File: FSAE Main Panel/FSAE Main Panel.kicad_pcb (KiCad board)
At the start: 2 copper layers, 3 parts

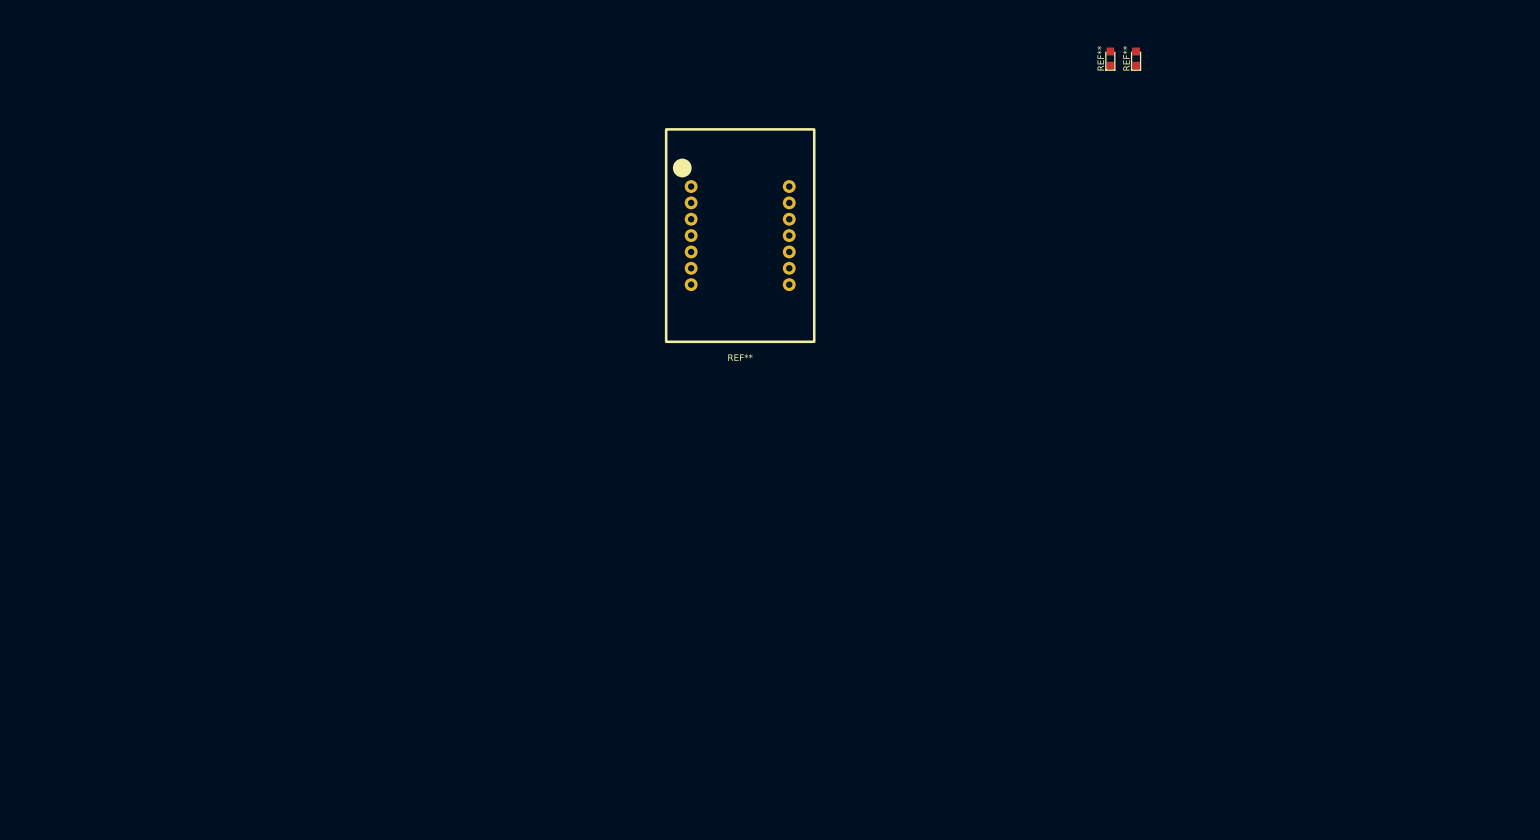
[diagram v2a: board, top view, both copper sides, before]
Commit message: Edited footprints, started PCB layout
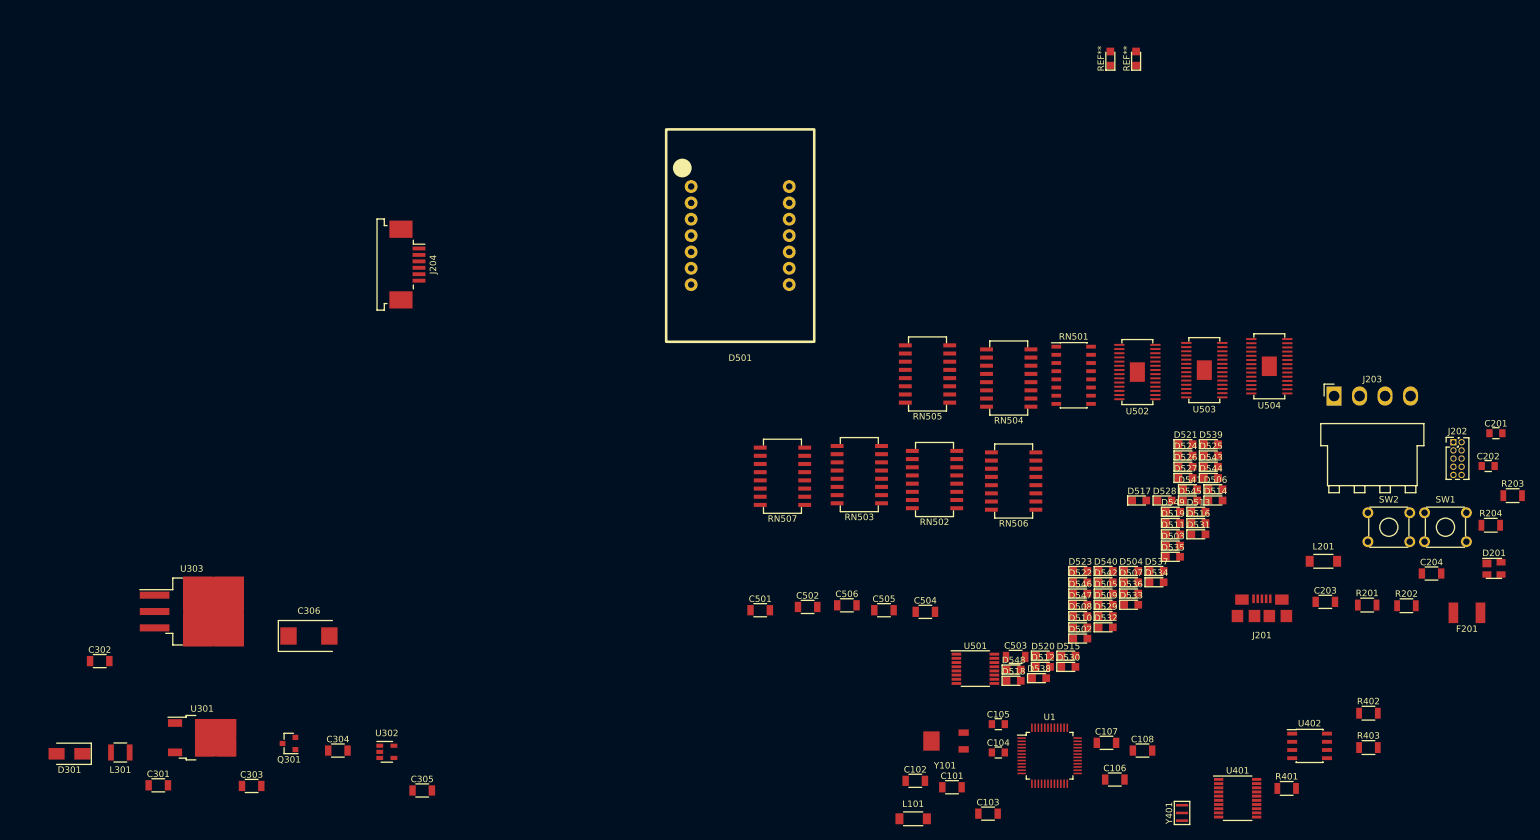
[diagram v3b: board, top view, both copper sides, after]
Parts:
- removed the REF** at (162.5, 65.5)
- added C101: 100nF, Capacitors_SMD:C_1206, F.Cu at (195.4, 151.2)
- added C102: 10uF, Capacitors_SMD:C_1206, F.Cu at (189.7, 150.2)
- added C103: 100nF, Capacitors_SMD:C_1206, F.Cu at (201.0, 155.3)
- added C104: 6.8pF, Capacitors_SMD:C_0805, F.Cu at (202.6, 145.8)
- added C105: 6.8pF, Capacitors_SMD:C_0805, F.Cu at (202.6, 141.4)
- added C106: 100nF, Capacitors_SMD:C_1206, F.Cu at (220.7, 150.0)
- added C107: 100nF, Capacitors_SMD:C_1206, F.Cu at (219.4, 144.3)
- added C108: 100nF, Capacitors_SMD:C_1206, F.Cu at (225.0, 145.5)
- added C201: 100pF, Capacitors_SMD:C_0805, F.Cu at (279.9, 96.2)
- added C202: 100pF, Capacitors_SMD:C_0805, F.Cu at (278.7, 101.3)
- added C203: 4.7nF, Capacitors_SMD:C_1206, F.Cu at (253.4, 122.4)
- added C204: 4.7nF, Capacitors_SMD:C_1206, F.Cu at (269.9, 118.0)
- added C301: 4.7uF, Capacitors_SMD:C_1206, F.Cu at (72.1, 150.9)
- added C302: 10uF, Capacitors_SMD:C_1206, F.Cu at (63.0, 131.6)
- added C303: 4.7uF, Capacitors_SMD:C_1206, F.Cu at (86.6, 151.0)
- added C304: 47uF, Capacitors_SMD:C_1206, F.Cu at (100.0, 145.5)
- added C305: 4.7uF, Capacitors_SMD:C_1206, F.Cu at (113.1, 151.7)
- added C306: 100uF, Capacitors_Tantalum_SMD:CP_Tantalum_Case-D_EIA-7343-31_Reflow, F.Cu at (95.5, 127.7)
- added C501: 1uF, Capacitors_SMD:C_1206, F.Cu at (165.6, 123.7)
- added C502: 100nF, Capacitors_SMD:C_1206, F.Cu at (173.0, 123.2)
- added C503: 4.7uF, Capacitors_SMD:C_1206, F.Cu at (205.3, 131.0)
- added C504: 100nF, Capacitors_SMD:C_1206, F.Cu at (191.3, 124.0)
- added C505: 100nF, Capacitors_SMD:C_1206, F.Cu at (184.8, 123.7)
- added C506: 100nF, Capacitors_SMD:C_1206, F.Cu at (179.1, 122.9)
- added D201: PRTR5V0U2X, TO_SOT_Packages_SMD:SOT-143, F.Cu at (279.6, 117.2)
- added D301: BYS10-45-E3/TR, Diodes_SMD:D_SMA, F.Cu at (58.3, 146.0)
- added D501: SA10-11GWA, Kingbright:SC10-11EWA, F.Cu at (162.5, 65.5)
- added D502: LG R971, LEDs:LED_0805, F.Cu at (215.3, 128.1)
- added D503: LG R971, LEDs:LED_0805, F.Cu at (229.7, 113.7)
- added D504: LG R971, LEDs:LED_0805, F.Cu at (223.2, 117.6)
- added D505: LG R971, LEDs:LED_0805, F.Cu at (219.3, 121.1)
- added D506: LG R971, LEDs:LED_0805, F.Cu at (236.3, 104.9)
- added D507: LG R971, LEDs:LED_0805, F.Cu at (223.2, 119.4)
- added D508: LG R971, LEDs:LED_0805, F.Cu at (215.3, 124.6)
- added D509: LG R971, LEDs:LED_0805, F.Cu at (219.3, 122.9)
- added D510: LG R971, LEDs:LED_0805, F.Cu at (215.3, 126.4)
- added D511: LG R971, LEDs:LED_0805, F.Cu at (229.7, 111.9)
- added D512: LG R971, LEDs:LED_0805, F.Cu at (209.5, 132.5)
- added D513: LG R971, LEDs:LED_0805, F.Cu at (233.7, 108.4)
- added D514: LG R971, LEDs:LED_0805, F.Cu at (236.3, 106.7)
- added D515: LG R971, LEDs:LED_0805, F.Cu at (213.5, 130.8)
- added D516: LG R971, LEDs:LED_0805, F.Cu at (233.7, 110.2)
- added D517: LG R971, LEDs:LED_0805, F.Cu at (224.5, 106.7)
- added D518: LY R976, LEDs:LED_0805, F.Cu at (205.0, 134.7)
- added D519: LY R976, LEDs:LED_0805, F.Cu at (229.7, 110.2)
- added D520: LY R976, LEDs:LED_0805, F.Cu at (209.5, 130.8)
- added D521: LY R976, LEDs:LED_0805, F.Cu at (231.7, 97.9)
- added D522: LY R976, LEDs:LED_0805, F.Cu at (215.3, 119.4)
- added D523: LY R976, LEDs:LED_0805, F.Cu at (215.3, 117.6)
- added D524: LY R976, LEDs:LED_0805, F.Cu at (231.7, 99.7)
- added D525: LY R976, LEDs:LED_0805, F.Cu at (235.6, 99.7)
- added D526: LS R976, LEDs:LED_0805, F.Cu at (231.7, 101.4)
- added D527: LS R976, LEDs:LED_0805, F.Cu at (231.7, 103.2)
- added D528: LS R976, LEDs:LED_0805, F.Cu at (228.4, 106.7)
- added D529: LS R976, LEDs:LED_0805, F.Cu at (219.3, 124.6)
- added D530: LS R976, LEDs:LED_0805, F.Cu at (213.5, 132.5)
- added D531: LS R976, LEDs:LED_0805, F.Cu at (233.7, 111.9)
- added D532: LS R976, LEDs:LED_0805, F.Cu at (219.3, 126.4)
- added D533: LS R976, LEDs:LED_0805, F.Cu at (223.2, 122.9)
- added D534: LB M673, LEDs:LED_0805, F.Cu at (227.2, 119.4)
- added D535: LB M673, LEDs:LED_0805, F.Cu at (229.7, 115.4)
- added D536: LB M673, LEDs:LED_0805, F.Cu at (223.2, 121.1)
- added D537: LB M673, LEDs:LED_0805, F.Cu at (227.2, 117.6)
- added D538: LB M673, LEDs:LED_0805, F.Cu at (208.9, 134.3)
- added D539: LB M673, LEDs:LED_0805, F.Cu at (235.6, 97.9)
- added D540: LB M673, LEDs:LED_0805, F.Cu at (219.3, 117.6)
- added D541: LB M673, LEDs:LED_0805, F.Cu at (232.4, 104.9)
- added D542: LB M673, LEDs:LED_0805, F.Cu at (219.3, 119.4)
- added D543: LB M673, LEDs:LED_0805, F.Cu at (235.6, 101.4)
- added D544: LB M673, LEDs:LED_0805, F.Cu at (235.6, 103.2)
- added D545: LB M673, LEDs:LED_0805, F.Cu at (232.4, 106.7)
- added D546: LB M673, LEDs:LED_0805, F.Cu at (215.3, 121.1)
- added D547: LB M673, LEDs:LED_0805, F.Cu at (215.3, 122.9)
- added D548: LB M673, LEDs:LED_0805, F.Cu at (205.0, 132.9)
- added D549: LB M673, LEDs:LED_0805, F.Cu at (229.7, 108.4)
- added F201: MF-MSMF050-2, MF-MSMF050-2:MF-MSMF050-2, F.Cu at (275.4, 124.1)
- added J201: USB Micro B, 10118192-0001LF:10118192-0001LF, F.Cu at (243.6, 124.6)
- added J202: Cortex_Debug, Pin_Headers:Pin_Header_Straight_2x05_Pitch1.27mm, F.Cu at (273.3, 97.6)
- added J203: Conn_01x04, Connectors_JST:JST_VH_B4PS-VH_2x4x3.96mm_Horizontal, F.Cu at (254.8, 90.4)
- added J204: TE_84953-6_FPC, Connectors_TE-Connectivity:TE_84953-6_1x06_P1.0mm_Horizontal, F.Cu at (110.8, 70.0)
- added L101: BLM41PG471SN1L, Inductors_SMD:L_1806, F.Cu at (189.4, 156.1)
- added L201: BLM41PG471SN1L, Inductors_SMD:L_1806, F.Cu at (253.1, 116.1)
- added L301: 742792310 Ferrite Bead, Inductors_SMD:L_1210, F.Cu at (66.2, 145.8)
- added Q301: IRLML6402TRPBF, TO_SOT_Packages_SMD:SOT-23, F.Cu at (92.4, 144.4)
- added R201: 10K, Resistors_SMD:R_1206, F.Cu at (259.9, 122.9)
- added R202: 330, Resistors_SMD:R_1206, F.Cu at (266.0, 123.0)
- added R203: 10K, Resistors_SMD:R_1206, F.Cu at (282.5, 105.9)
- added R204: 330, Resistors_SMD:R_1206, F.Cu at (279.1, 110.5)
- added R401: 10k, Resistors_SMD:R_1206, F.Cu at (247.4, 151.4)
- added R402: 10k, Resistors_SMD:R_1206, F.Cu at (260.1, 139.7)
- added R403: 120, Resistors_SMD:R_1206, F.Cu at (260.1, 145.0)
- added RN501: 51 Ohm (8x), Housings_SOIC:SOIC-16_3.9x9.9mm_Pitch1.27mm, F.Cu at (214.3, 87.2)
- added RN502: 151 Ohm (8x), Bourns 4800P:Bourns 4800P SOM-16, F.Cu at (192.7, 103.4)
- added RN503: 151 Ohm (8x), Bourns 4800P:Bourns 4800P SOM-16, F.Cu at (181.0, 102.6)
- added RN504: 220 Ohm (8x), Bourns 4800P:Bourns 4800P SOM-16, F.Cu at (204.2, 87.6)
- added RN505: 180 Ohm (8x), Bourns 4800P:Bourns 4800P SOM-16, F.Cu at (191.6, 87.0)
- added RN506: 68 Ohm (8x), Bourns 4800P:Bourns 4800P SOM-16, F.Cu at (205.0, 103.6)
- added RN507: 68 Ohm (8x), Bourns 4800P:Bourns 4800P SOM-16, F.Cu at (169.1, 102.9)
- added SW1: B3W-1020, Buttons_Switches_THT:SW_TH_Tactile_Omron_B3F-10xx, F.Cu at (268.8, 108.6)
- added SW2: B3W-1020, Buttons_Switches_THT:SW_TH_Tactile_Omron_B3F-10xx, F.Cu at (260.0, 108.6)
- added U1: SAMD21G18A-AU, Housings_QFP:TQFP-48_7x7mm_Pitch0.5mm, F.Cu at (210.6, 146.3)
- added U301: ZLDO1117-5V, TO_SOT_Packages_SMD:TO-252-2, F.Cu at (78.9, 143.5)
- added U302: LP2985-3.3, TO_SOT_Packages_SMD:SOT-23-5, F.Cu at (107.6, 145.7)
- added U303: LM1085-5.0, TO_SOT_Packages_SMD:TO-263-3_TabPin2, F.Cu at (77.3, 123.9)
- added U401: MCP2515-I/ST, Housings_SSOP:TSSOP-20_4.4x6.5mm_Pitch0.65mm, F.Cu at (239.8, 152.9)
- added U402: MCP2551-I/SN, Housings_SOIC:SOIC-8_3.9x4.9mm_Pitch1.27mm, F.Cu at (251.0, 144.8)
- added U501: TLC6C598, Housings_SSOP:TSSOP-16_4.4x5mm_Pitch0.65mm, F.Cu at (199.0, 132.8)
- added U502: TLC6C5816, TLC6C5816:TLC6C5816, F.Cu at (224.2, 86.7)
- added U503: TLC6C5816, TLC6C5816:TLC6C5816, F.Cu at (234.6, 86.4)
- added U504: TLC6C5816, TLC6C5816:TLC6C5816, F.Cu at (244.7, 85.8)
- added Y101: 32.768kHz, MS1V-T1K:MS1V-T1K, F.Cu at (194.3, 144.0)
- added Y401: Resonator, CSTNE16M0V530000R0:CSTNE16M0V530000R0, F.Cu at (231.1, 155.2)

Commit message: Placed LEDs on PCB
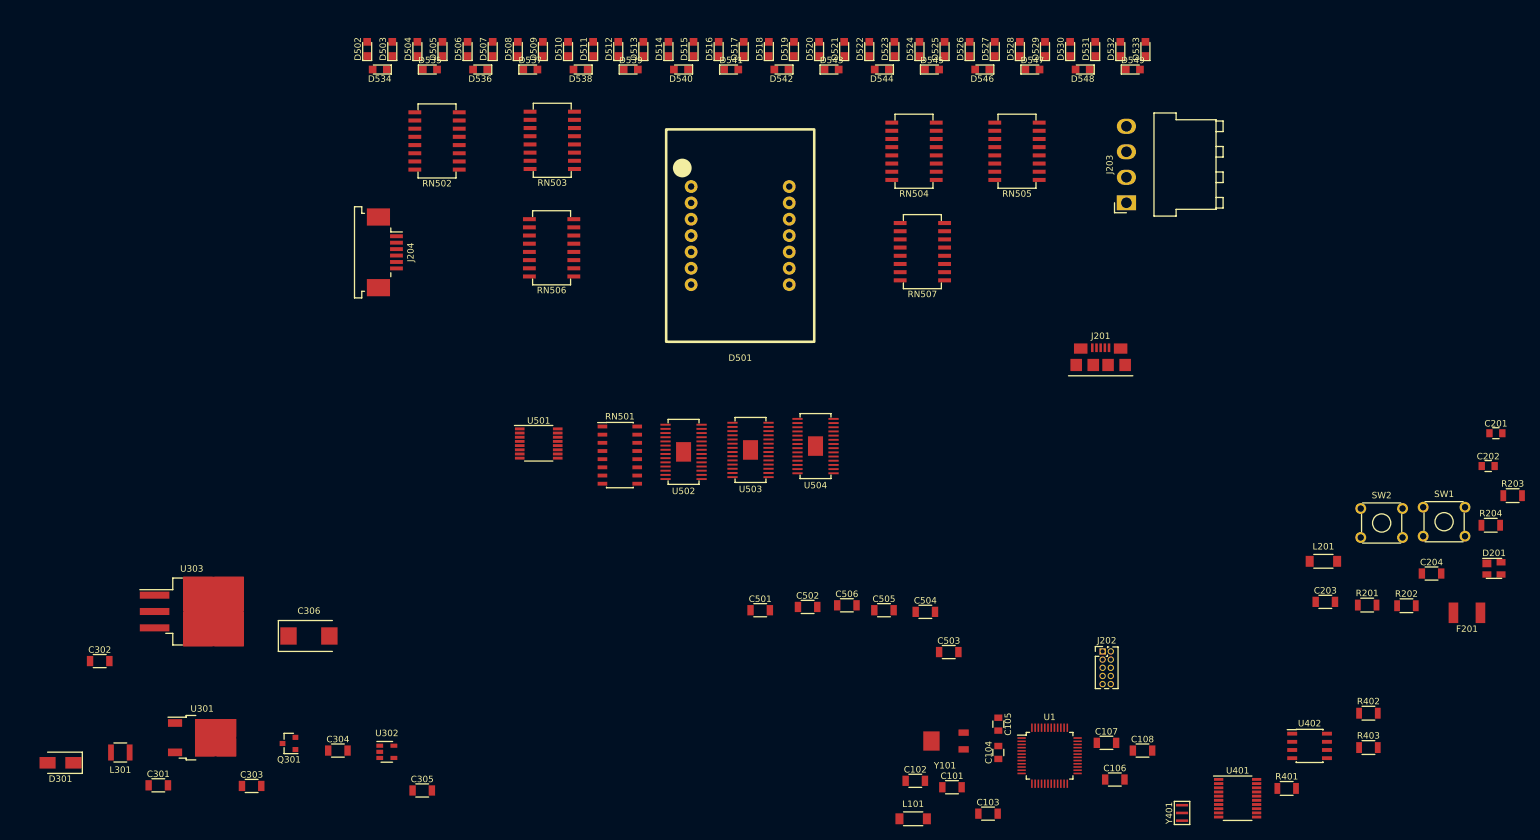
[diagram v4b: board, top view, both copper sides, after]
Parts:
- removed REF** (x2): LED_0805, LEDs:LED_0805
- moved D534 144.6 mm to (106.5, 39.7), turned to 180 degrees
- moved D502 143.8 mm to (104.5, 36.5), turned to 90 degrees
- moved D503 143.7 mm to (108.5, 36.5), turned to 90 degrees
- moved D535 138.0 mm to (114.3, 39.7)
- moved D504 137.4 mm to (112.3, 36.5), turned to 90 degrees
- moved D506 134.8 mm to (120.2, 36.5), turned to 90 degrees
- moved D505 133.3 mm to (116.2, 36.5), turned to 90 degrees
- moved D536 129.8 mm to (122.1, 39.7), turned to 180 degrees
- moved D507 129.2 mm to (124.0, 36.5), turned to 90 degrees
- moved D537 124.6 mm to (129.9, 39.7)
- moved D508 124.1 mm to (128.0, 36.5), turned to 90 degrees
- moved D509 122.9 mm to (131.8, 36.5), turned to 90 degrees
- moved D510 120.0 mm to (135.8, 36.5), turned to 90 degrees
- moved D538 118.4 mm to (137.7, 39.7), turned to 180 degrees
- moved D511 117.5 mm to (139.7, 36.5), turned to 90 degrees
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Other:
- board text added: "Maximum length 160mm"
- board text added: "Maximum width 55mm"
